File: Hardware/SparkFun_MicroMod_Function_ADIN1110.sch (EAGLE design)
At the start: 88 parts, among them J1 IP20(RJ50), J2 MICROMOD_FUNCTION_STANDARD, Q1 220mA/50V/3.5Ω, Q2 20V/4.2A/52mΩ/1.4W, T1 WE-STST, U1 ADIN1110, U2 EEPROM, U3 3.3V, U4 WE-TVS, Y1 25MHz

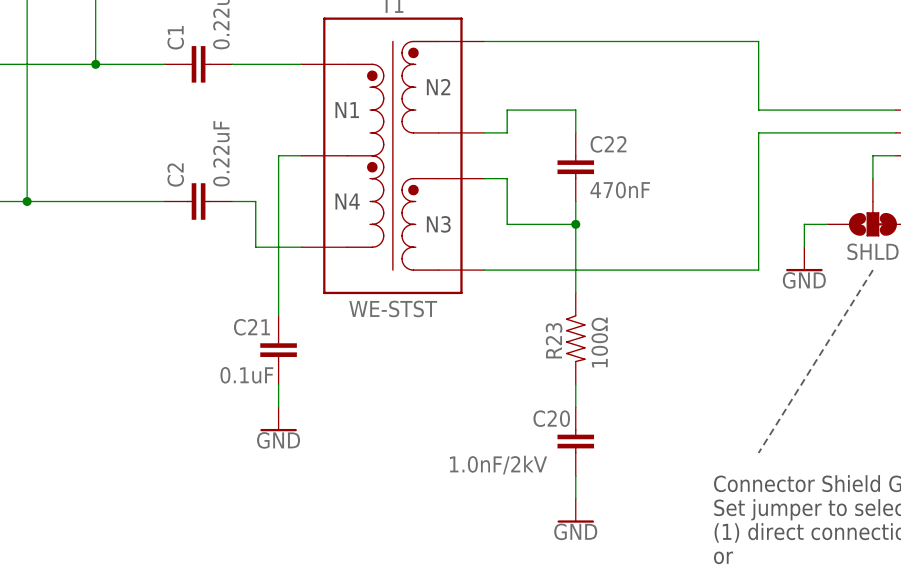
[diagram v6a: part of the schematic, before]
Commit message: 470pF cap to 0805 with new PROD_ID
-new 470nF cap had to bump up to 0805 for the 100V rating in that value
-Voltage specs in part values
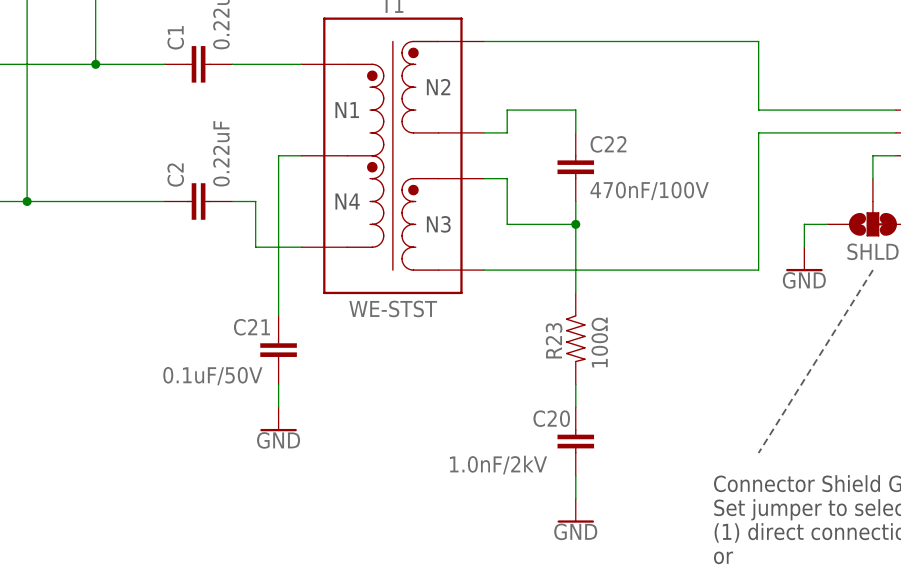
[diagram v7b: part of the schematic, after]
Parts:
- C21: value 0.1uF -> 0.1uF/50V
- C22: value 470nF -> 470nF/100V; device SparkFun-Capacitors:470NF-0603-10V-10%-X5R -> SparkFun-Capacitors:470NF-0805-100V-10%-X7S
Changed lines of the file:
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@@
 <part name="C20" library="SparkFun-Capacitors" deviceset="1.0NF/1000PF" device="-1206-2KV-10%-X7R-WORTH-ELEKRONIK" value="1.0nF/2kV"/>
 <part name="R23" library="SparkFun-Resistors" deviceset="100OHM" device="-0603-1/10W-1%" value="100Ω"/>
-<part name="C21" library="SparkFun-Capacitors" deviceset="0.1UF" device="-0603-50V-10%-X7R-WE" value="0.1uF"/>
-<part name="C22" library="SparkFun-Capacitors" deviceset="470NF" device="-0603-10V-10%-X5R" value="470nF"/>
+<part name="C21" library="SparkFun-Capacitors" deviceset="0.1UF" device="-0603-50V-10%-X7R-WE" value="0.1uF/50V"/>
+<part name="C22" library="SparkFun-Capacitors" deviceset="470NF" device="-0805-100V-10%-X7S" value="470nF/100V"/>
 <part name="GND14" library="SparkFun-PowerSymbols" deviceset="GND" device=""/>
 <part name="LED-LINK" library="SparkFun-Jumpers" deviceset="JUMPER-SMT_2_NC_TRACE" device="_SILK" package3d_urn="urn:adsk.eagle:package:39281/1" value="JUMPER-SMT_2_NC_TRACE_SILK"/>
@@
 <instance part="C21" gate="G$1" x="254" y="172.72" smashed="yes">
 <attribute name="NAME" x="248.92" y="175.641" size="1.778" layer="95" font="vector"/>
-<attribute name="VALUE" x="247.396" y="170.307" size="1.778" layer="96" font="vector"/>
+<attribute name="VALUE" x="241.046" y="170.307" size="1.778" layer="96" font="vector"/>
 </instance>
 <instance part="C22" gate="G$1" x="287.02" y="193.04" smashed="yes">

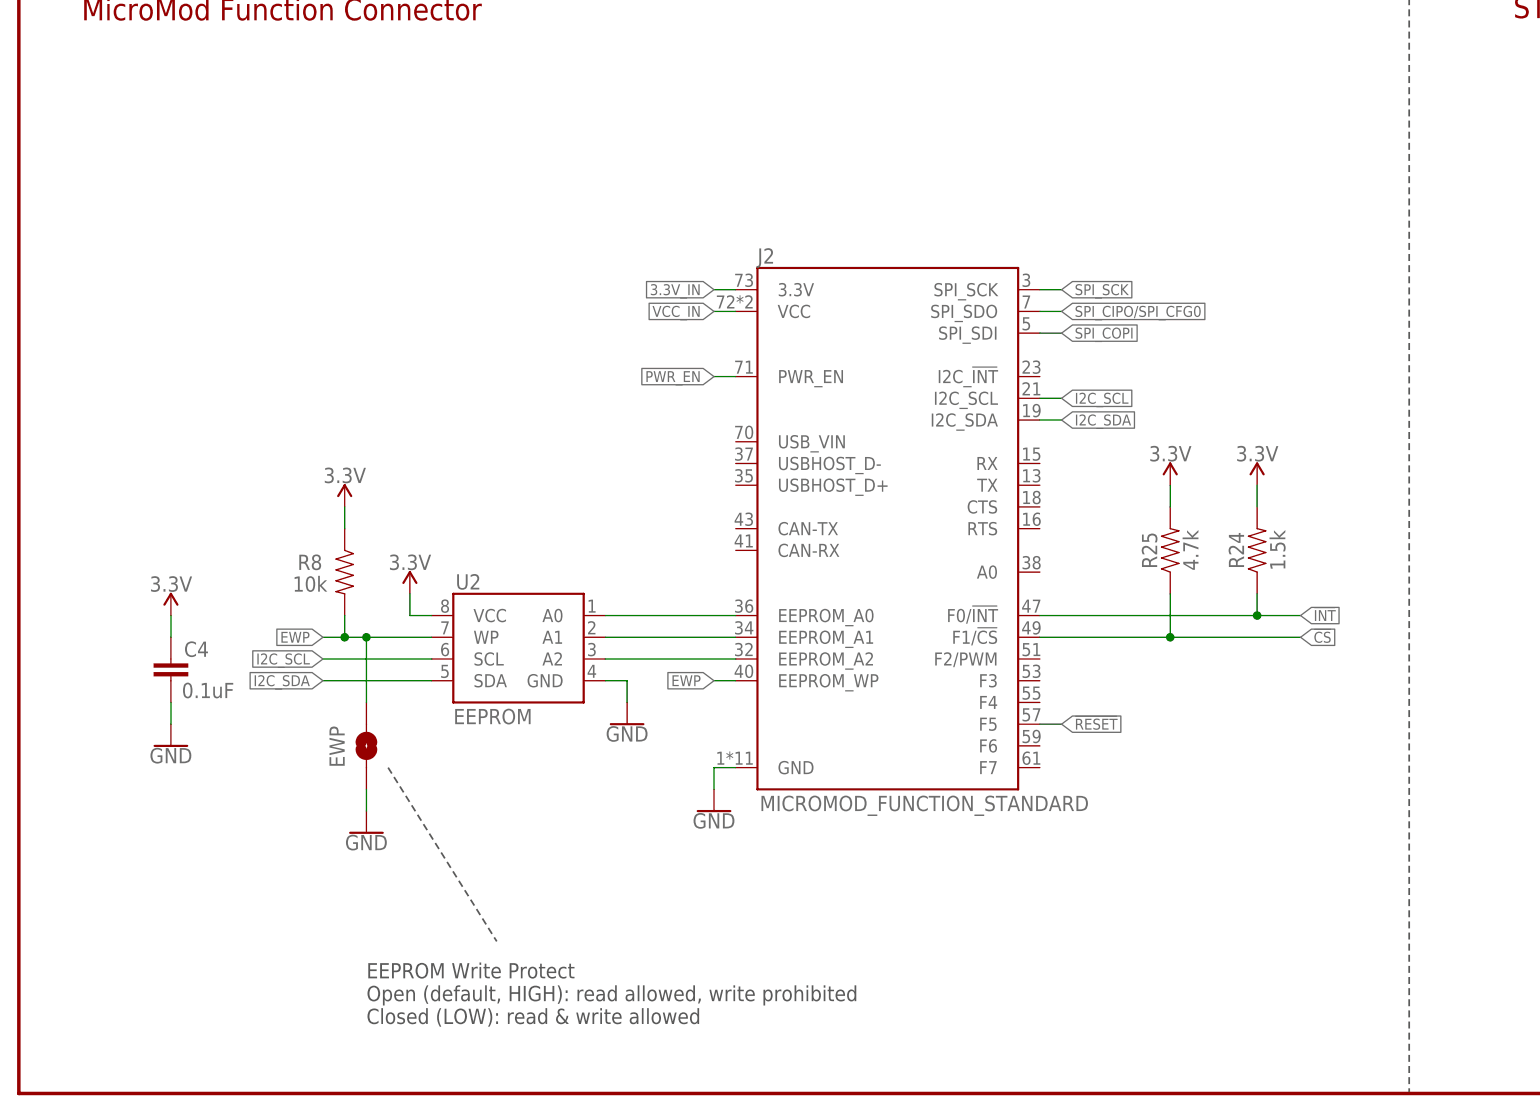
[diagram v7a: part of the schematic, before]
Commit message: SPI test points and moved config jumpers
-moved bottom config jumpers to avoid reflections on CIPO
-added SPI test points
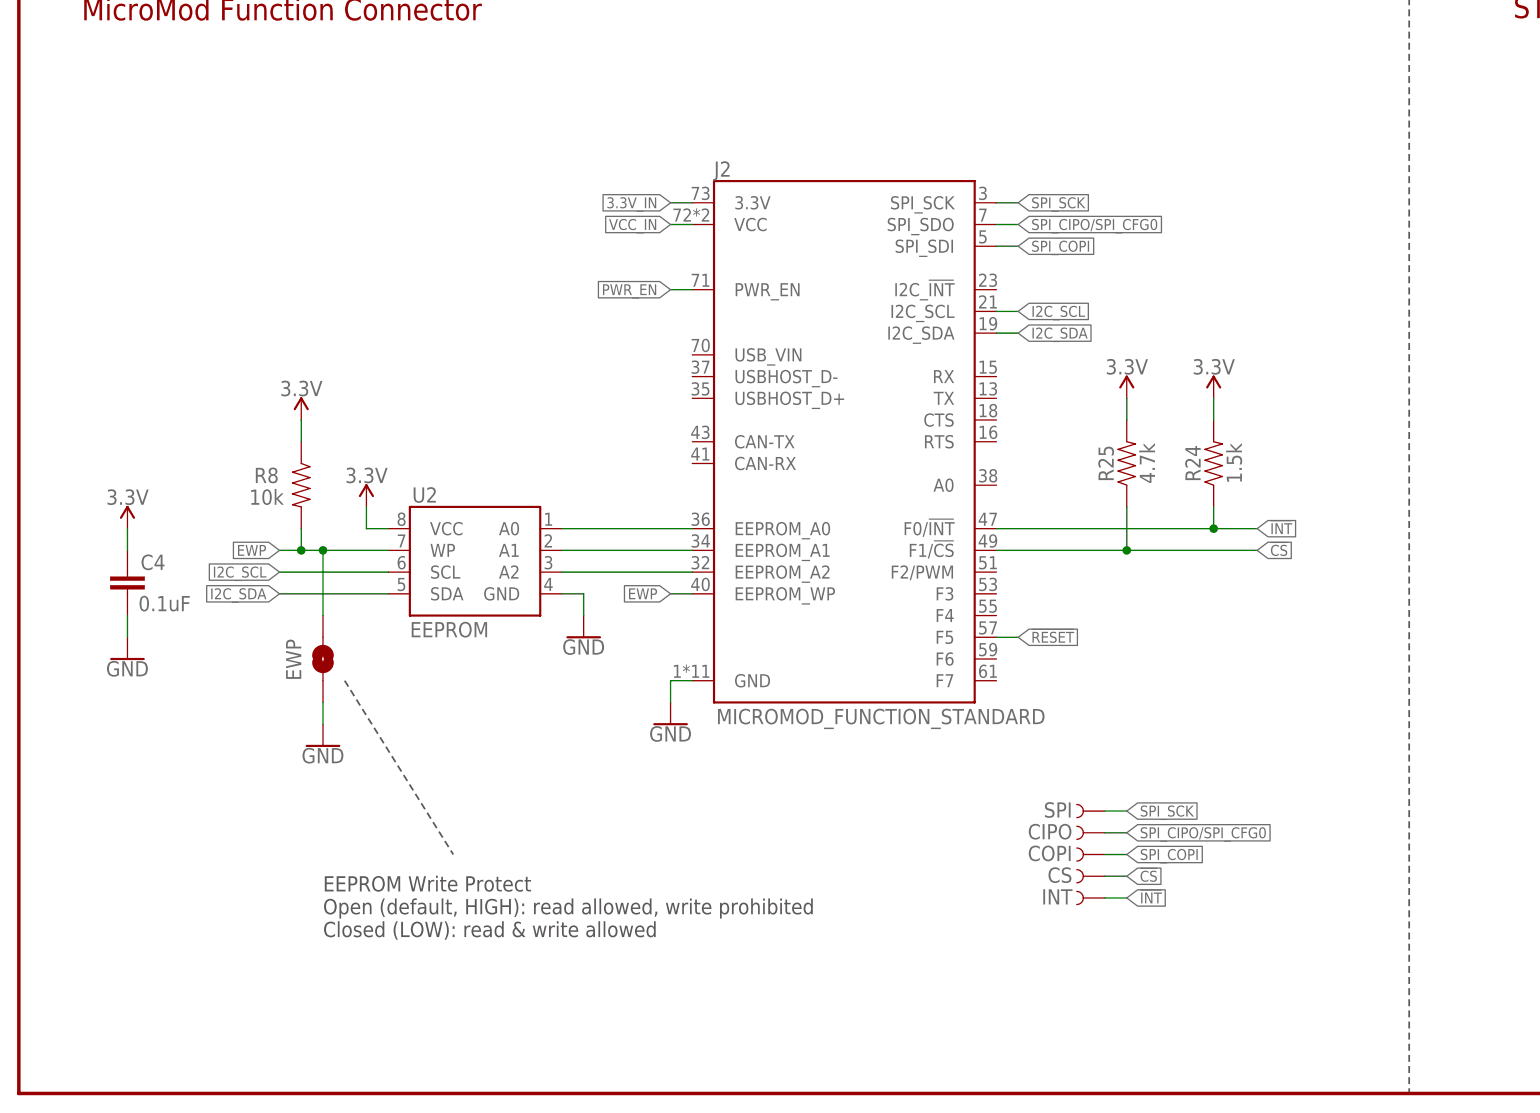
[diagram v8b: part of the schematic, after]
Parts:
- added CIPO, COPI, CS, INT, SPI: TEST-POINTTP_15TH_THRU, SparkFun-Connectors:TEST-POINTTP_15TH_THRU
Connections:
- net !CS!: now also CS.1
- net !INT!: now also INT.1
- net SPI_CIPO/SPI_CFG0: now also CIPO.1
- net SPI_COPI: now also COPI.1
- net SPI_SCK: now also SPI.1
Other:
- moved on the sheet: C4, EWP, J2, R24, R25, R8, U2
